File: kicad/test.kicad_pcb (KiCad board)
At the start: 2 copper layers, 117.5 x 38.5 mm, 8 parts, among them SW10 SW_Push_Dual, SW11 SW_Push_Dual, SW12 SW_Push_Dual, SW9 SW_Push_Dual, U2 ESP32-S3-WROOM-1

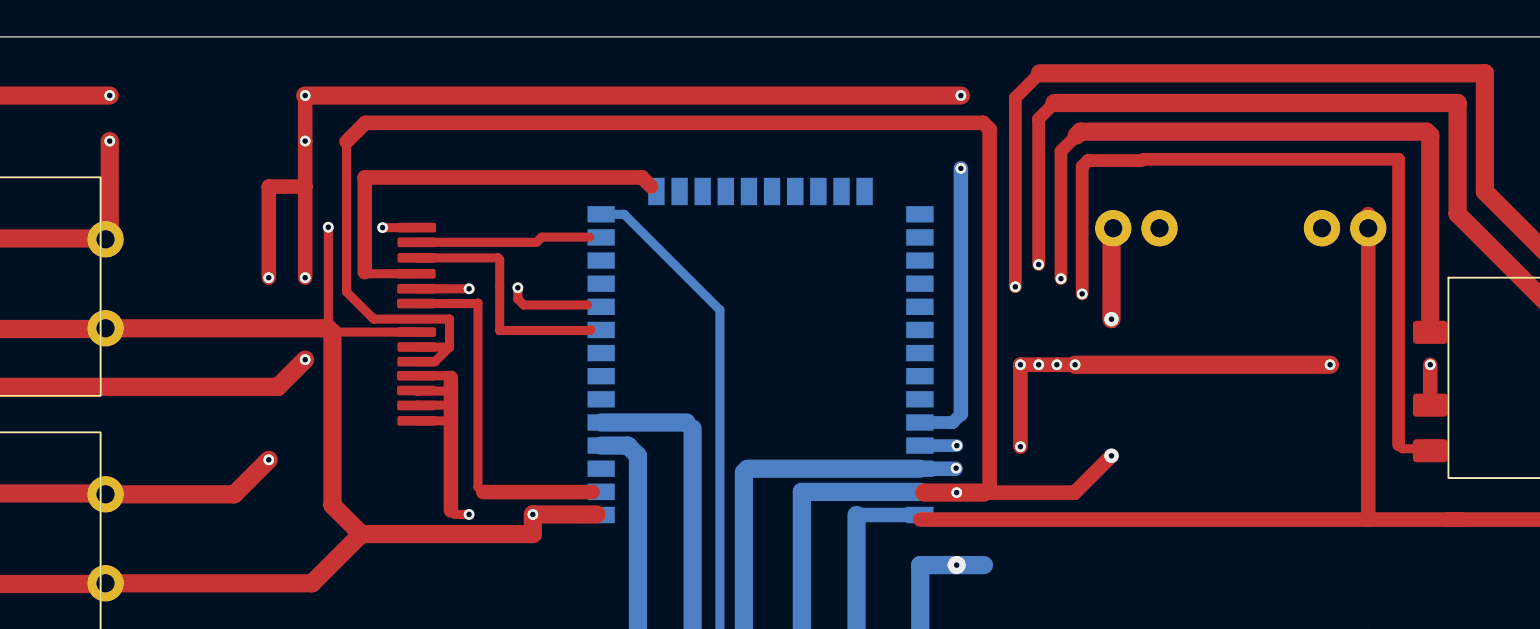
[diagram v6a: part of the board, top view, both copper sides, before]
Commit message: add more text in kicad
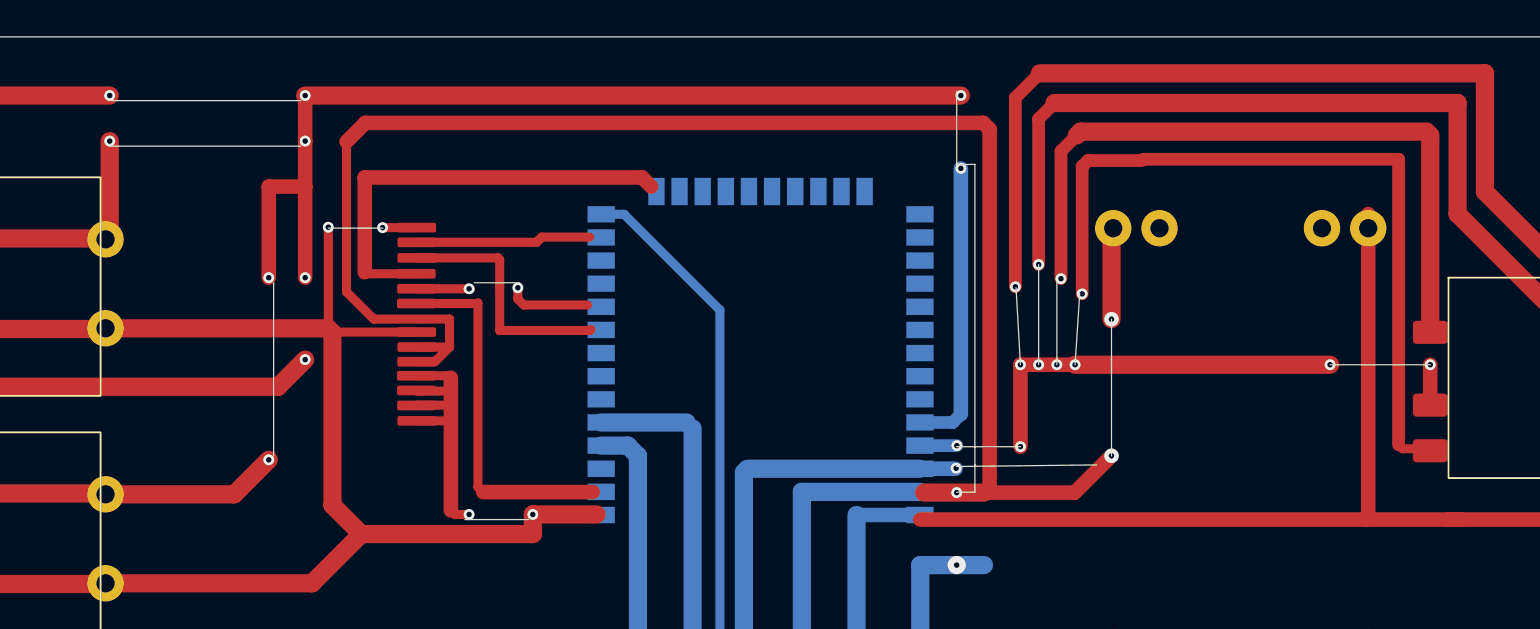
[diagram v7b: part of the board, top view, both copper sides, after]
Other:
- outline, holes or cut-outs redrawn
- board text added: "0 OM"
- board text added: "1 KOM"
- board text added: "10 KOM"
- board text added: "2.2 KOM"
- board text added: "2.2KOM"
- board text added: "20 KOM"
- board text added: "200 OM"
- board text added: "3V3"
- board text added: "4.7 KOM"
- board text added: "BUTTON SWITCH"
- board text added: "EN"
- board text added: "GND"
- board text added: "IO12 TO BUTTON GND"
- board text added: "RX"
- board text added: "TX"
